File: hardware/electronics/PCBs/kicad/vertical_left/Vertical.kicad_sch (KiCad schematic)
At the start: 0 parts

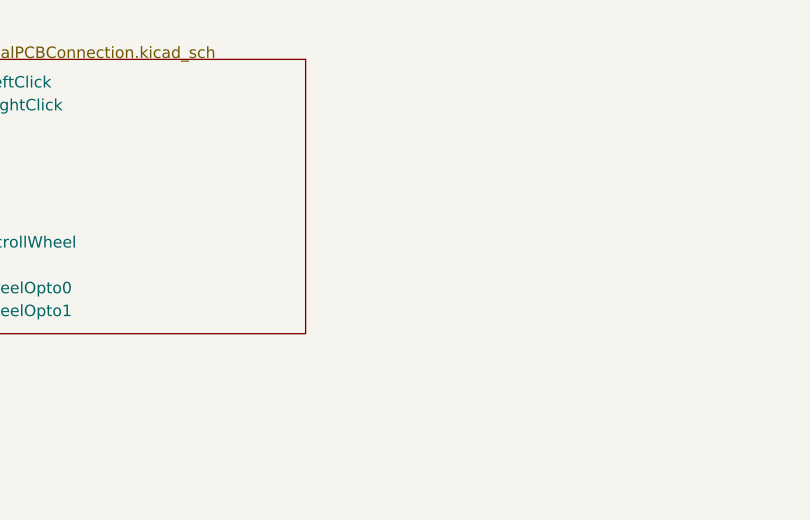
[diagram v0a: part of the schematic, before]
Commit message: Vertical neopixels
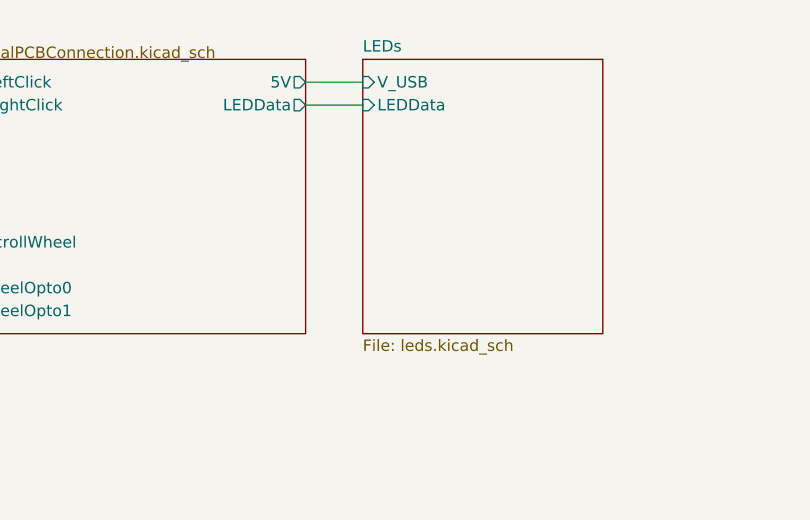
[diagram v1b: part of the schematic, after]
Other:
- added sheet LEDs (leds.kicad_sch)
- sheet VPC ports: added 5V, LEDData; removed none
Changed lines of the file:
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@@
+		)
+	)
+	(wire
+		(pts
+			(xy 193.04 88.9) (xy 199.39 88.9)
+		)
+		(stroke
+			(width 0)
+			(type default)
 		)
 	)
@@
 			(type solid)
 			(color 0 0 0 1)
+		)
+	)
+	(wire
+		(pts
+			(xy 193.04 86.36) (xy 199.39 86.36)
+		)
+		(stroke
+			(width 0)
+			(type default)
 		)
 	)
@@
 			)
 		)
+		(pin "5V" output
+			(at 193.04 86.36 0)
+			(effects
+				(font
+					(size 1.27 1.27)
+				)
+				(justify right)
+			)
+		)
+		(pin "LEDData" output
+			(at 193.04 88.9 0)
+			(effects
+				(font
+					(size 1.27 1.27)
+				)
+				(justify right)
+			)
+		)
 		(instances
 			(project "Vertical"
@@
 				)
 			)
+		)
+	)
+	(sheet
+		(at 199.39 83.82)
+		(size 26.67 30.48)
+		(exclude_from_sim no)
+		(in_bom yes)
+		(on_board yes)
+		(dnp no)
+		(fields_autoplaced yes)
+		(stroke
+			(width 0.1524)
+			(type solid)
+		)
+		(fill
+			(color 0 0 0 0)
+		)
+		(property "Sheetname" "LEDs"
+			(at 199.39 83.1084 0)
+			(show_name no)
+			(do_not_autoplace no)
+			(effects
+				(font
+					(size 1.27 1.27)
+				)
+				(justify left bottom)
+			)
+		)
+		(property "Sheetfile" "leds.kicad_sch"
+			(at 199.39 114.8846 0)
+			(show_name no)
+			(do_not_autoplace no)
+			(effects
+				(font
+					(size 1.27 1.27)
+				)
+				(justify left top)
+			)
+		)
+		(pin "LEDData" input
+			(at 199.39 88.9 180)
+			(effects
+				(font
+					(size 1.27 1.27)
+				)
+				(justify left)
+			)
+		)
+		(pin "V_USB" input
+			(at 199.39 86.36 180)
+			(effects
+				(font
+					(size 1.27 1.27)
+				)
+				(justify left)
+			)
+		)
+		(instances
+			(project "Vertical"
+				(path "/ddf7ec59-41eb-40e8-9c32-f8edbc666fb4"
+					(page "1")
+				)
+			)
